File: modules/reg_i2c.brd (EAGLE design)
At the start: 25.4 x 12.4 mm, 11 parts, among them U1 P82B715D

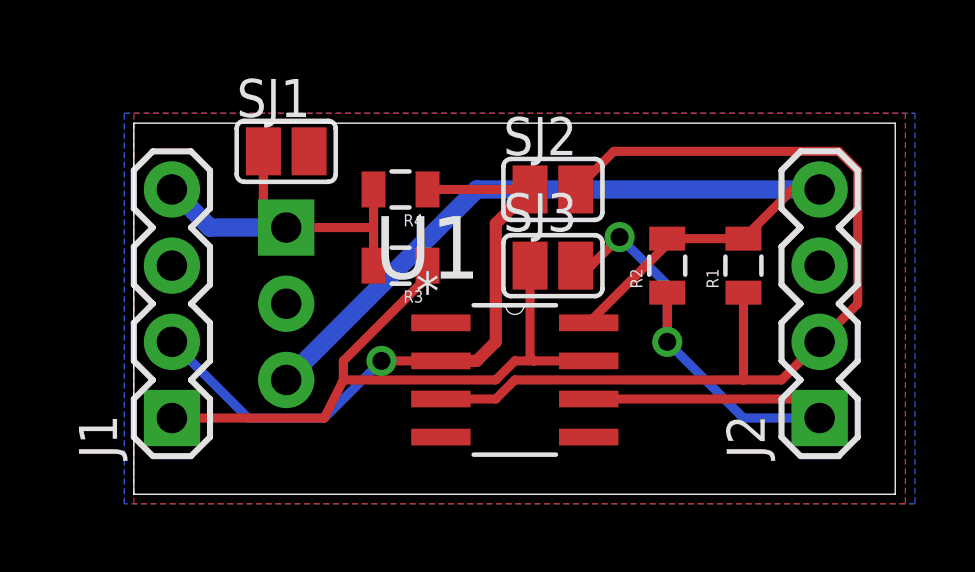
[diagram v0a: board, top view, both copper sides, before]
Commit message: V1.0 initial design complete of Regulator board
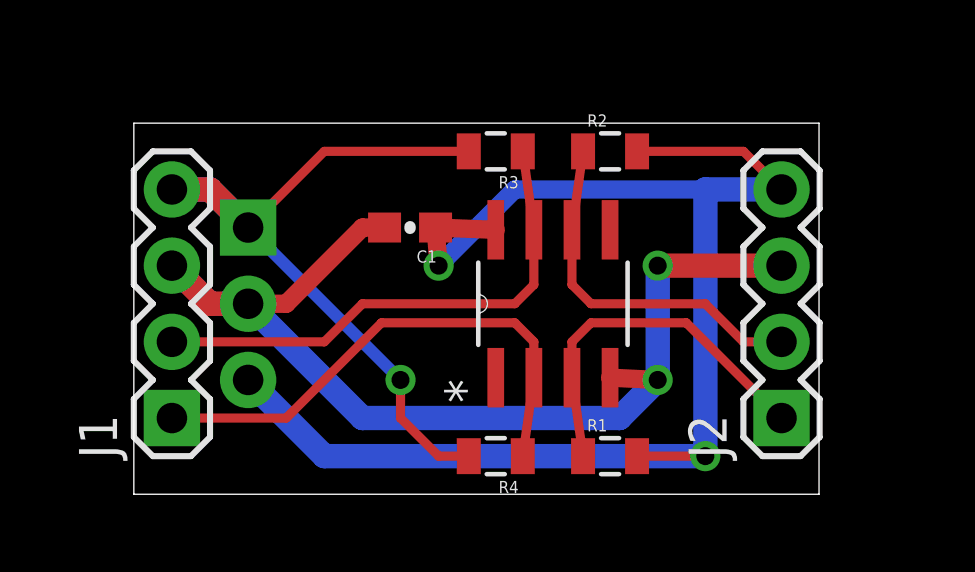
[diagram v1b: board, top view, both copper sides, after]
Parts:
- removed SJ1, SJ2, SJ3: (no value), jumper:SJ
- added C1: 2.2uF, SparkFun-Capacitors:0603-CAP
- moved R4 9.44 mm to (12.1, 1.27)
- moved R1 7.75 mm to (15.9, 1.27), turned to 0 degrees
- moved R3 4.96 mm to (12.1, 11.4)
- moved R2 4.26 mm to (15.9, 11.4), turned to 0 degrees
- moved U1 2.84 mm to (14.0, 6.35), turned to 90 degrees
- moved RG1 1.27 mm to (3.81, 6.35)
- moved J2 1.27 mm to (21.6, 2.54)
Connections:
- removed net N$3: J2.2, R1.1, SJ2.2, U1.3
- removed net N$4: J2.1, R2.1, SJ3.2, U1.6
- new net N$6: J1.2, R3.1, U1.7
- new net N$7: J1.1, R4.1, U1.2
- net 12V: no longer SJ1.1
- net 5V: now also C1.1; no longer SJ1.2
- net GND: now also C1.2
- net N$1: now also J2.1, R1.1, U1.3; no longer J1.2, R4.1, SJ2.1, U1.2
- net N$2: now also J2.2, R2.1, U1.6; no longer J1.1, R3.1, SJ3.1, U1.7
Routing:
- net GND: track 0.00 -> 37.0 mm, vias 0 -> 2
- net N$3: track 32.8 -> 0.00 mm
- net N$4: track 21.7 -> 0.00 mm, vias 2 -> 0
- net 5V: track 30.1 -> 48.6 mm, vias 0 -> 2
- net N$7: track 0.00 -> 17.5 mm
- net N$6: track 0.00 -> 17.3 mm
- net 12V: track 12.6 -> 25.8 mm, vias 0 -> 1
- net N$2: track 23.1 -> 12.2 mm
- net N$1: track 21.9 -> 12.4 mm, vias 1 -> 0
- removed copper zone on layer 16, net GND
- removed copper zone on layer 1, net N$5
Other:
- board size 25.4 x 12.4 mm -> 22.8 x 12.4 mm

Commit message: Added labels to pins on reg board
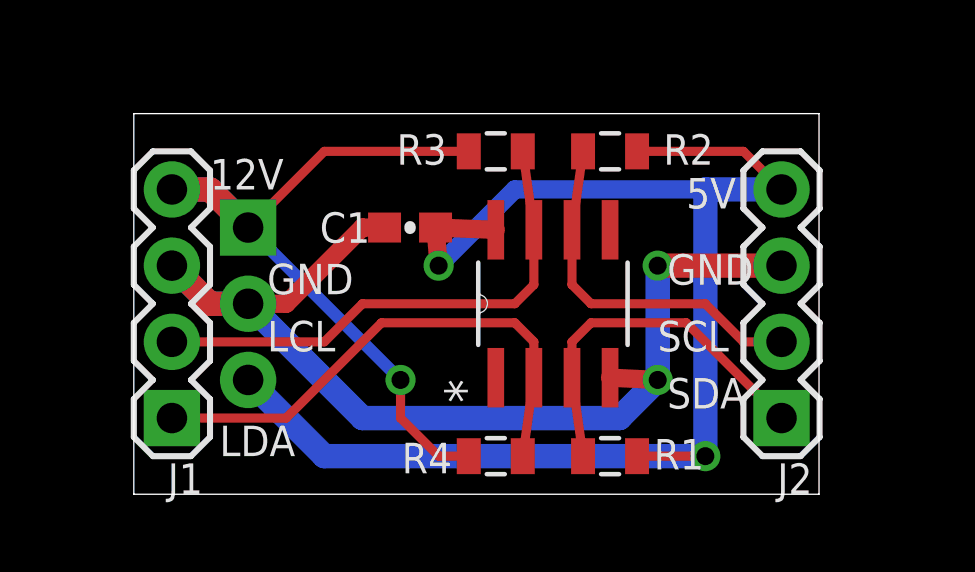
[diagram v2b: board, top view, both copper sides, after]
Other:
- board size 22.8 x 12.4 mm -> 22.8 x 12.7 mm
- board text added: "12V"
- board text added: "5V"
- board text added: "GND"
- board text added: "LCL"
- board text added: "LDA"
- board text added: "SCL"
- board text added: "SDA"
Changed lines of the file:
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@@
 <plain>
 <wire x1="0" y1="0" x2="22.84" y2="0" width="0" layer="20"/>
-<wire x1="22.84" y1="0" x2="22.84" y2="12.37" width="0" layer="20"/>
-<wire x1="22.84" y1="12.37" x2="0" y2="12.37" width="0" layer="20"/>
-<wire x1="0" y1="12.37" x2="0" y2="0" width="0" layer="20"/>
+<wire x1="22.84" y1="0" x2="22.84" y2="12.6875" width="0" layer="20"/>
+<wire x1="22.84" y1="12.6875" x2="0" y2="12.6875" width="0" layer="20"/>
+<wire x1="0" y1="12.6875" x2="0" y2="0" width="0" layer="20"/>
+<text x="2.54" y="10.16" size="1.016" layer="21" font="vector" ratio="15">12V</text>
+<text x="20.0025" y="9.525" size="1.016" layer="22" font="vector" ratio="15" rot="MR0">5V</text>
+<text x="5.08" y="10.16" size="1.016" layer="22" font="vector" ratio="15" rot="MR0">12V</text>
+<text x="20.0025" y="2.2225" size="1.016" layer="22" font="vector" ratio="15" rot="MR0">SDA</text>
+<text x="6.6675" y="4.7625" size="1.016" layer="22" font="vector" ratio="15" rot="MR0">LCL</text>
+<text x="5.3975" y="1.27" size="1.016" layer="22" font="vector" ratio="15" rot="MR0">LDA</text>
+<text x="20.0025" y="4.7625" size="1.016" layer="22" font="vector" ratio="15" rot="MR0">SCL</text>
+<text x="18.415" y="9.525" size="1.016" layer="21" font="vector" ratio="15">5V</text>
+<text x="17.4625" y="4.7625" size="1.016" layer="21" font="vector" ratio="15">SCL</text>
+<text x="17.78" y="2.8575" size="1.016" layer="21" font="vector" ratio="15">SDA</text>
+<text x="2.8575" y="1.27" size="1.016" layer="21" font="vector" ratio="15">LDA</text>
+<text x="4.445" y="4.7625" size="1.016" layer="21" font="vector" ratio="15">LCL</text>
+<text x="17.78" y="6.985" size="1.016" layer="21" font="vector" ratio="15">GND</text>
+<text x="4.445" y="6.6675" size="1.016" layer="21" font="vector" ratio="15">GND</text>
+<text x="20.32" y="6.985" size="1.016" layer="22" font="vector" ratio="15" rot="MR0">GND</text>
+<text x="6.985" y="6.6675" size="1.016" layer="22" font="vector" ratio="15" rot="MR0">GND</text>
 </plain>
 <attributes>
@@
 </autorouter>
 <elements>
-<element name="J1" library="SparkFun-Connectors" package="1X04" value="" x="1.27" y="2.54" rot="R90">
+<element name="J1" library="SparkFun-Connectors" package="1X04" value="" x="1.27" y="2.54" smashed="yes" rot="R90">
 <attribute name="PROD_ID" value="CONN-09696" x="1.27" y="2.54" size="1.778" layer="27" rot="R90" display="off"/>
-</element>
-<element name="J2" library="SparkFun-Connectors" package="1X04" value="" x="21.59" y="2.54" rot="R90">
+<attribute name="NAME" x="2.2987" y="1.0287" size="1.016" layer="25" font="vector" ratio="15" rot="R180"/>
+<attribute name="VALUE" x="4.445" y="1.27" size="1.27" layer="27" rot="R90"/>
+</element>
+<element name="J2" library="SparkFun-Connectors" package="1X04" value="" x="21.59" y="2.54" smashed="yes" rot="R90">
 <attribute name="PROD_ID" value="CONN-09696" x="21.59" y="2.54" size="1.778" layer="27" rot="R90" display="off"/>
-</element>
-<element name="R1" library="SparkFun-Resistors" package="0805" value="" x="15.875" y="1.27"/>
-<element name="R2" library="SparkFun-Resistors" package="0805" value="" x="15.875" y="11.43"/>
-<element name="R3" library="SparkFun-Resistors" package="0805" value="" x="12.065" y="11.43" rot="R180"/>
-<element name="R4" library="SparkFun-Resistors" package="0805" value="" x="12.065" y="1.27" rot="R180"/>
+<attribute name="NAME" x="22.6187" y="1.0287" size="1.016" layer="25" font="vector" ratio="15" rot="R180"/>
+<attribute name="VALUE" x="24.765" y="1.27" size="1.27" layer="27" rot="R90"/>
+</element>
+<element name="R1" library="SparkFun-Resistors" package="0805" value="" x="15.875" y="1.27" smashed="yes">
+<attribute name="NAME" x="17.3355" y="0.8255" size="1.016" layer="25" font="vector" ratio="15"/>
+<attribute name="VALUE" x="14.859" y="-0.127" size="0.4064" layer="27"/>
+</element>
+<element name="R2" library="SparkFun-Resistors" package="0805" value="" x="15.875" y="11.43" smashed="yes">
+<attribute name="NAME" x="17.653" y="10.9855" size="1.016" layer="25" font="vector" ratio="15"/>
+<attribute name="VALUE" x="14.859" y="10.033" size="0.4064" layer="27"/>
+</element>
+<element name="R3" library="SparkFun-Resistors" package="0805" value="" x="12.065" y="11.43" smashed="yes" rot="R180">
+<attribute name="NAME" x="8.763" y="10.9855" size="1.016" layer="25" font="vector" ratio="15"/>
+<attribute name="VALUE" x="13.081" y="12.827" size="0.4064" layer="27" rot="R180"/>
+</element>
+<element name="R4" library="SparkFun-Resistors" package="0805" value="" x="12.065" y="1.27" smashed="yes" rot="R180">
+<attribute name="NAME" x="10.6045" y="1.7145" size="1.016" layer="25" font="vector" ratio="15" rot="R180"/>
+<attribute name="VALUE" x="13.081" y="2.667" size="0.4064" layer="27" rot="R18"/>
+</element>
 <element name="RG1" library="Puffin" package="MURATA_REG_HOR" value="" x="3.81" y="6.35" smashed="yes" rot="MR90">
-<attribute name="NAME" x="5.0038" y="0.5588" size="1.016" layer="26" font="vector" ratio="15" rot="MR90"/>
+<attribute name="NAME" x="10.8712" y="5.0038" size="1.016" layer="26" font="vector" ratio="15" rot="MR0"/>
 <attribute name="VALUE" x="10.795" y="3.81" size="1.016" layer="28" font="vector" ratio="15" rot="MR90"/>
 </element>
@@
 <attribute name="OC_FARNELL" value="1604945" x="13.97" y="6.35" size="1.778" layer="27" rot="R90" display="off"/>
 </element>
-<element name="C1" library="SparkFun-Capacitors" package="0603-CAP" value="2.2uF" x="9.2075" y="8.89" rot="R180">
+<element name="C1" library="SparkFun-Capacitors" package="0603-CAP" value="2.2uF" x="9.2075" y="8.89" smashed="yes" rot="R180">
 <attribute name="PROD_ID" value="CAP-07888" x="9.2075" y="8.89" size="1.778" layer="27" rot="R180" display="off"/>
+<attribute name="NAME" x="7.874" y="9.398" size="1.016" layer="25" font="vector" ratio="15" rot="R180"/>
+<attribute name="VALUE" x="10.2235" y="10.033" size="0.4064" layer="27" font="vector" rot="R180"/>
 </element>
 </elements>
